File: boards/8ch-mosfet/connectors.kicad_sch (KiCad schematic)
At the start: 30 parts, among them J1 N2K, J2 I2C

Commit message: more routing and layout
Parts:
- removed R4 (x2): 2.2k, Resistor_SMD:R_0805_2012Metric_Pad1.20x1.40mm_HandSolder, symbol Device:R_Small_US
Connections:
- net GNDD: now also J1.3 (Pin_3), J2.3 (Pin_3); no longer J1.4 (Pin_4), J2.4 (Pin_4)
- net at C1.1, D30.2 (A2), FB5.1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: no longer D31.2 (A2)
- net at C1.1, FB6.1: now also D31.2 (A2), J1.4 (Pin_4); no longer J1.3 (Pin_3)
- net at C1.1, D27.2 (A2), FB2.1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: no longer D28.2 (A2)
- net at C1.1, FB3.1: now also D28.2 (A2), J2.4 (Pin_4); no longer J2.3 (Pin_3)
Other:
- moved on the sheet: D1, D27, D28, D29, D30, D31

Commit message: more or less placed all the stuff that needs to be placed
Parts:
- removed R4 (x2): 2.2k, Resistor_SMD:R_0805_2012Metric_Pad1.20x1.40mm_HandSolder, symbol Device:R_Small_US
- added R4 (x2): 2.2k, Resistor_SMD:R_0805_2012Metric_Pad1.20x1.40mm_HandSolder, symbol Device:R_Small_US
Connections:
- net +3.3V: now also R4.2, R4.2
- net SCL: now also R4.1
- net SDA: now also R4.1

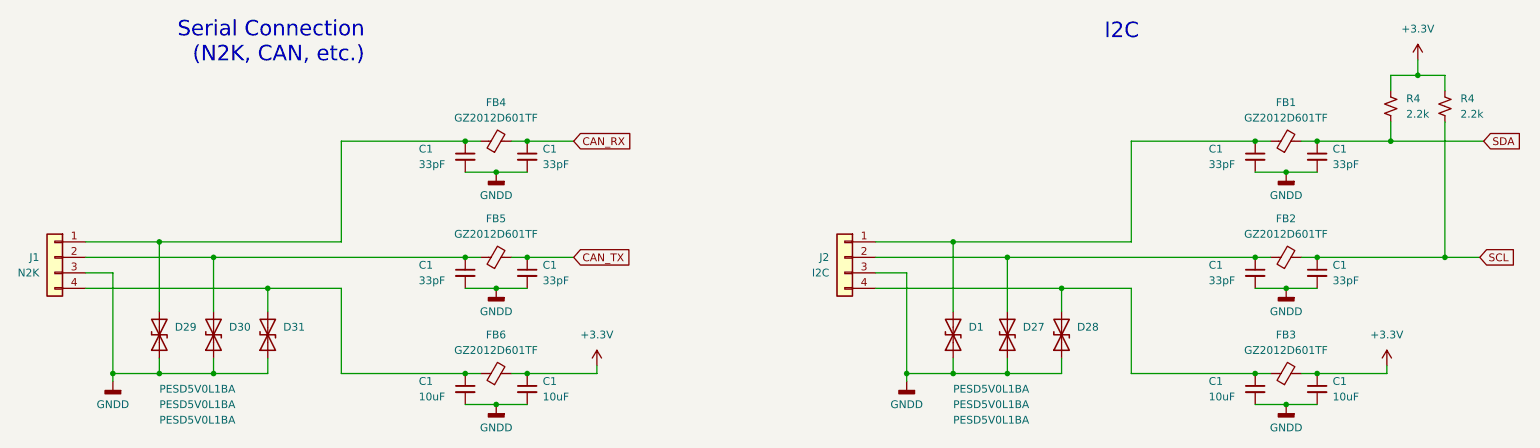
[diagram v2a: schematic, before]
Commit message: tidied up the schematic
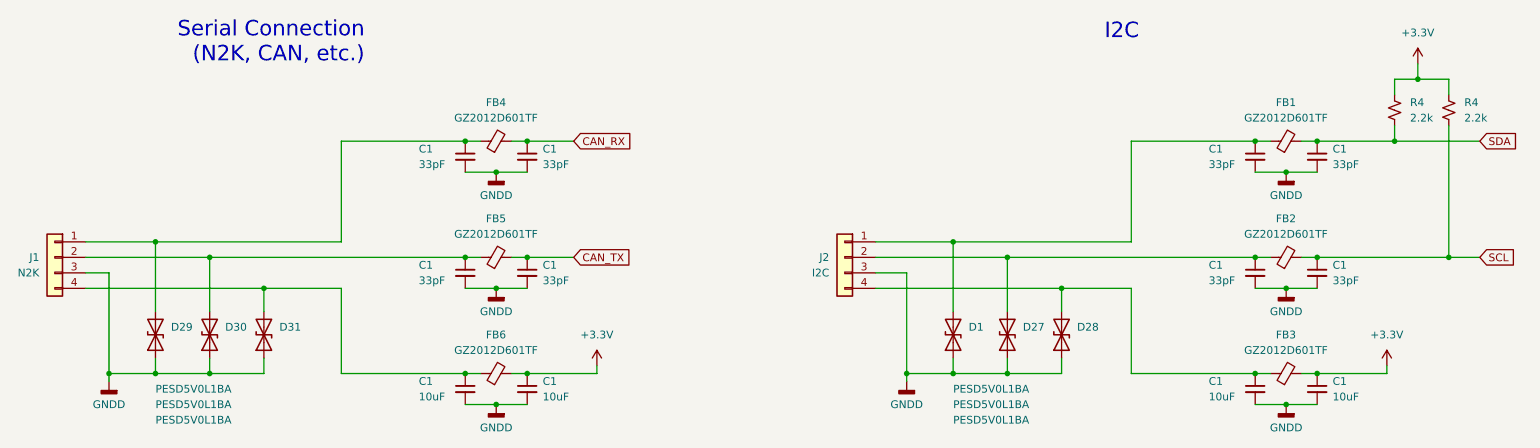
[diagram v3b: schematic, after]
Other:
- moved on the sheet: D29, D30, D31, R4

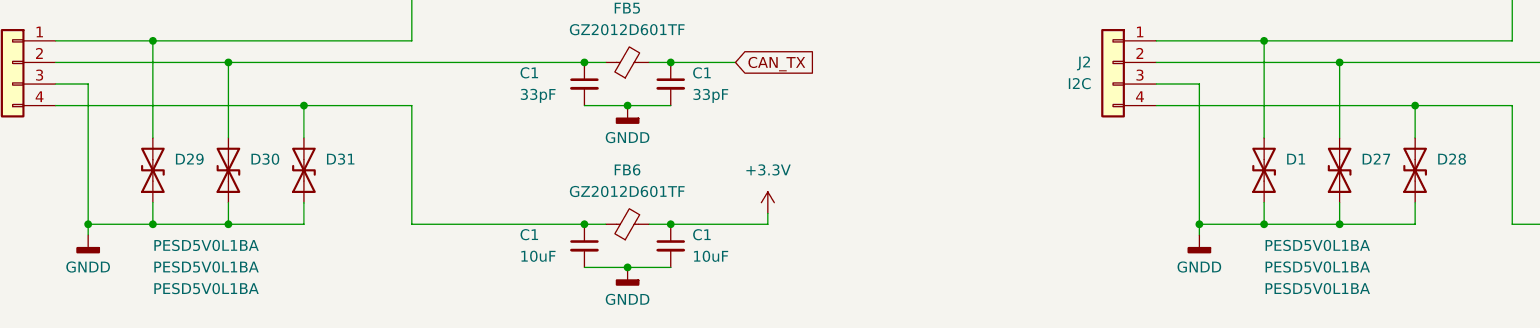
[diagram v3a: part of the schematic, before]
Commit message: fixed a part number
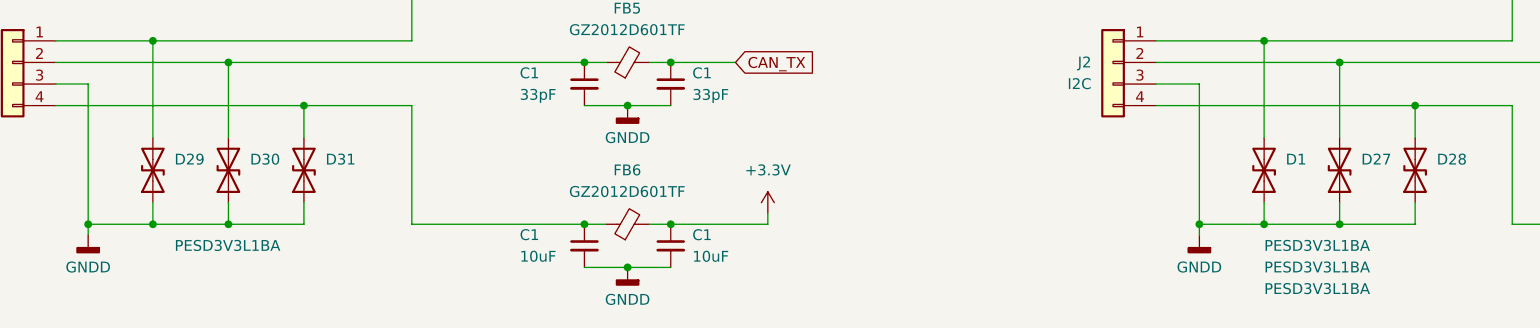
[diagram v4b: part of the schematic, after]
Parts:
- D1, D27, D28, D29, D30, D31: value PESD5V0L1BA -> PESD3V3L1BA
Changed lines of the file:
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@@
       (effects (font (size 1.27 1.27)) (justify right))
     )
-    (property "Value" "PESD5V0L1BA" (at 52.07 105.41 90)
-      (effects (font (size 1.27 1.27)) (justify right))
+    (property "Value" "PESD3V3L1BA" (at 52.07 105.41 90)
+      (effects (font (size 1.27 1.27)) (justify right) hide)
     )
     (property "Footprint" "Diode_SMD:D_SOD-323_HandSoldering" (at 60.96 93.98 0)
@@
       (effects (font (size 1.27 1.27)) (justify right))
     )
-    (property "Value" "PESD5V0L1BA" (at 52.07 102.87 90)
+    (property "Value" "PESD3V3L1BA" (at 54.61 102.87 90)
       (effects (font (size 1.27 1.27)) (justify right))
     )
@@
       (effects (font (size 1.27 1.27)) (justify right))
     )
-    (property "Value" "PESD5V0L1BA" (at 182.88 107.95 90)
+    (property "Value" "PESD3V3L1BA" (at 182.88 107.95 90)
       (effects (font (size 1.27 1.27)) (justify right))
     )
@@
       (effects (font (size 1.27 1.27)) (justify right))
     )
-    (property "Value" "PESD5V0L1BA" (at 182.88 102.87 90)
+    (property "Value" "PESD3V3L1BA" (at 182.88 102.87 90)
       (effects (font (size 1.27 1.27)) (justify right))
     )
@@
       (effects (font (size 1.27 1.27)) (justify right))
     )
-    (property "Value" "PESD5V0L1BA" (at 182.88 105.41 90)
+    (property "Value" "PESD3V3L1BA" (at 182.88 105.41 90)
       (effects (font (size 1.27 1.27)) (justify right))
     )
@@
       (effects (font (size 1.27 1.27)) (justify right))
     )
-    (property "Value" "PESD5V0L1BA" (at 52.07 107.95 90)
-      (effects (font (size 1.27 1.27)) (justify right))
+    (property "Value" "PESD3V3L1BA" (at 52.07 107.95 90)
+      (effects (font (size 1.27 1.27)) (justify right) hide)
     )
     (property "Footprint" "Diode_SMD:D_SOD-323_HandSoldering" (at 69.85 93.98 0)

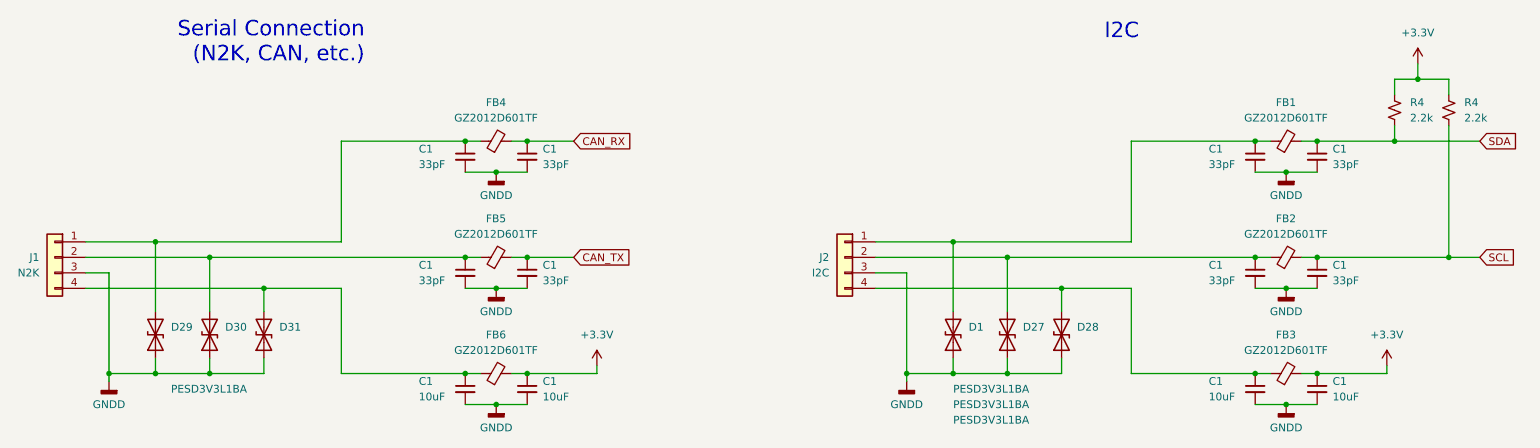
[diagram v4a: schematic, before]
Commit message: changed back to qwiic and moved it under the esp32
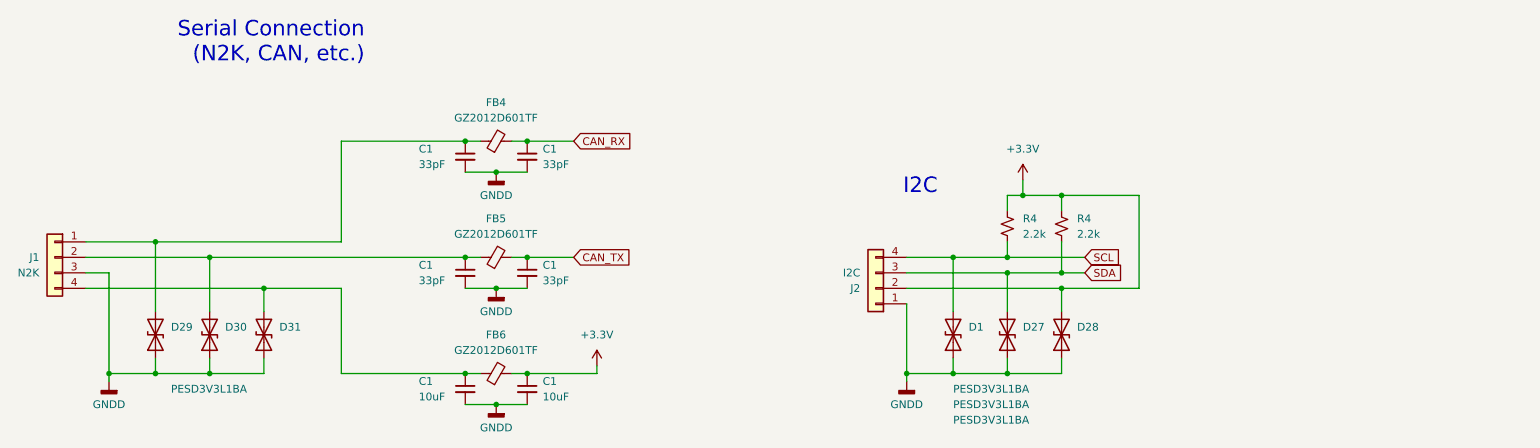
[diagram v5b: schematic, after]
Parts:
- removed C1 (x4): 33pF, Capacitor_SMD:C_0805_2012Metric_Pad1.18x1.45mm_HandSolder, symbol Device:C_Small
- removed C1 (x2): 10uF, Capacitor_SMD:C_0805_2012Metric_Pad1.18x1.45mm_HandSolder, symbol Device:C_Small
- removed FB1, FB2, FB3: GZ2012D601TF, Inductor_SMD:L_0805_2012Metric, symbol Device:FerriteBead_Small
- J2: footprint Connector_PinHeader_2.54mm:PinHeader_1x04_P2.54mm_Vertical -> Connector_JST:JST_SH_SM04B-SRSS-TB_1x04-1MP_P1.00mm_Horizontal; Vendor (none) -> SM04B-SRSS-TB
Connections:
- net +3.3V: now also D28.2 (A2), J2.2 (Pin_2)
- net GNDD: now also J2.1 (Pin_1); no longer J2.3 (Pin_3)
- net SCL: now also D1.2 (A2), J2.4 (Pin_4), R4.1; no longer R4.1
- net SDA: now also D27.2 (A2), J2.3 (Pin_3), R4.1; no longer R4.1
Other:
- moved on the sheet: J2, R4

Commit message: updated layout with new fuse.
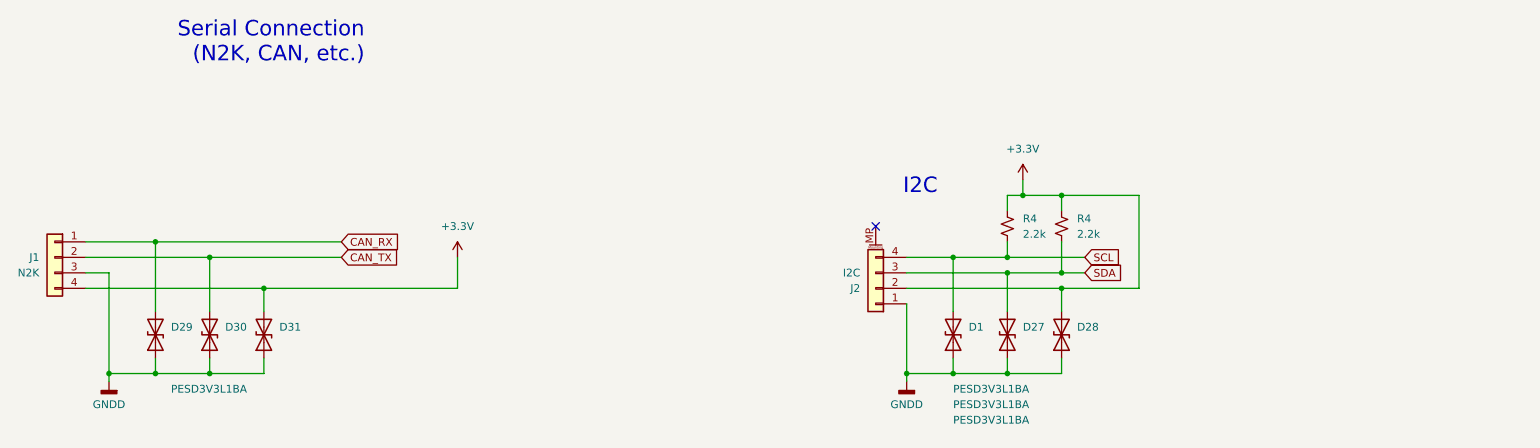
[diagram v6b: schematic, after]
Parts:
- removed C1 (x4): 33pF, Capacitor_SMD:C_0805_2012Metric_Pad1.18x1.45mm_HandSolder, symbol Device:C_Small
- removed C1 (x2): 10uF, Capacitor_SMD:C_0805_2012Metric_Pad1.18x1.45mm_HandSolder, symbol Device:C_Small
- removed FB4, FB5, FB6: GZ2012D601TF, Inductor_SMD:L_0805_2012Metric, symbol Device:FerriteBead_Small
- J2: symbol Connector_Generic:Conn_01x04 -> Connector_Generic_MountingPin:Conn_01x04_MountingPin
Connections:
- net +3.3V: now also D31.2 (A2), J1.4 (Pin_4)
- net CAN_RX: now also D29.2 (A2), J1.1 (Pin_1)
- net CAN_TX: now also D30.2 (A2), J1.2 (Pin_2)
- no-connect marks 0 -> 1

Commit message: prepared 8ch mosfet for production
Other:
- company: (none) -> https://github.com/hoeken/yarrboard
- title: (none) -> Yarrboard 8ch Mosfet Driver
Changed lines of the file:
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@@
 (kicad_sch (version 20230121) (generator eeschema)
   (paper "A4")
+  (title_block
+    (title "Yarrboard 8ch Mosfet Driver")
+    (company "https://github.com/hoeken/yarrboard")
+  )
   (junction (at 191.77 83.82) (diameter 0) (color 0 0 0 0)
   )

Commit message: updated BOM
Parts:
- D1, D27, D28, D29, D30, D31: LCSC (none) -> C316020
- J2: LCSC (none) -> C160404; Vendor SM04B-SRSS-TB -> (none)
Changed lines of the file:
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@@
+      (effects (font (size 1.27 1.27)) hide)
+    )
+    (property "LCSC" "C316020" (at 60.96 93.98 90)
       (effects (font (size 1.27 1.27)) hide)
     )
@@
     )
     (property "Datasheet" "~" (at 52.07 93.98 0)
+      (effects (font (size 1.27 1.27)) hide)
+    )
+    (property "LCSC" "C316020" (at 52.07 93.98 90)
       (effects (font (size 1.27 1.27)) hide)
     )
@@
       (effects (font (size 1.27 1.27)) hide)
     )
+    (property "LCSC" "C316020" (at 200.66 93.98 90)
+      (effects (font (size 1.27 1.27)) hide)
+    )
     (pin "1")
     (pin "2")
@@
     )
     (property "Datasheet" "~" (at 182.88 93.98 0)
+      (effects (font (size 1.27 1.27)) hide)
+    )
+    (property "LCSC" "C316020" (at 182.88 93.98 90)
       (effects (font (size 1.27 1.27)) hide)
     )
@@
       (effects (font (size 1.27 1.27)) hide)
     )
-    (property "Vendor" "SM04B-SRSS-TB" (at 170.18 86.36 0)
+    (property "LCSC" "C160404" (at 170.18 86.36 0)
       (effects (font (size 1.27 1.27)) hide)
     )
@@
       (effects (font (size 1.27 1.27)) hide)
     )
-    (property "Vendor" "" (at 200.66 76.2 0)
-      (effects (font (size 1.27 1.27)) hide)
-    )
     (pin "1")
     (pin "2")
@@
       (effects (font (size 1.27 1.27)) hide)
     )
-    (property "Vendor" "" (at 191.77 76.2 0)
-      (effects (font (size 1.27 1.27)) hide)
-    )
     (pin "1")
     (pin "2")
@@
       (effects (font (size 1.27 1.27)) hide)
     )
+    (property "LCSC" "C316020" (at 191.77 93.98 90)
+      (effects (font (size 1.27 1.27)) hide)
+    )
     (pin "1")
     (pin "2")
@@
       (effects (font (size 1.27 1.27)) hide)
     )
+    (property "LCSC" "C316020" (at 69.85 93.98 90)
+      (effects (font (size 1.27 1.27)) hide)
+    )
